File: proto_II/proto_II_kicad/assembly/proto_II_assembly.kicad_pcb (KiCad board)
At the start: 2 copper layers, 100 x 97 mm, 109 parts, among them J101 BOOT_CFG, J102 SNSR_I2C, J103 SNSR_PWR, J104 Vin, J105 RS485_A, J106 RS485_B, J107 ISO_GND, J108 Vin-5V, J109 SWD_DBG, J301 SIG_BYPASS, J302 PWR_BYPASS, SW101 RST, SW102 MODBUS_ADDR, SW103 USR_BTN, U101 STM32F103C8Tx, U201 TPS54331, U202 XC6206P332MR, U301 ADUM5241, U302 EL357N-G, U303 EL357N-G, U304 ST485EBDR, Y101 HSE, Y102 LSE

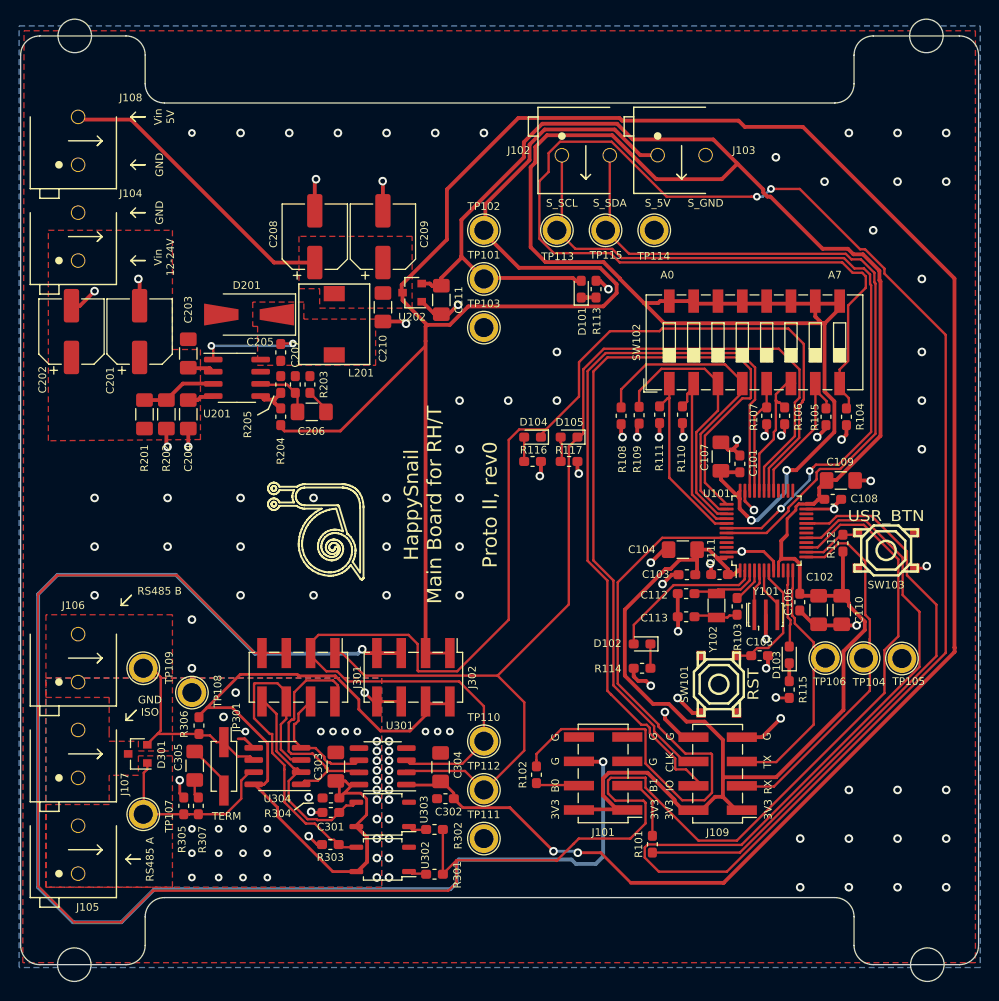
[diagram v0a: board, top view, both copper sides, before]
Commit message: Fix issues with rev.0 of MarkI board
Partially addresses #16
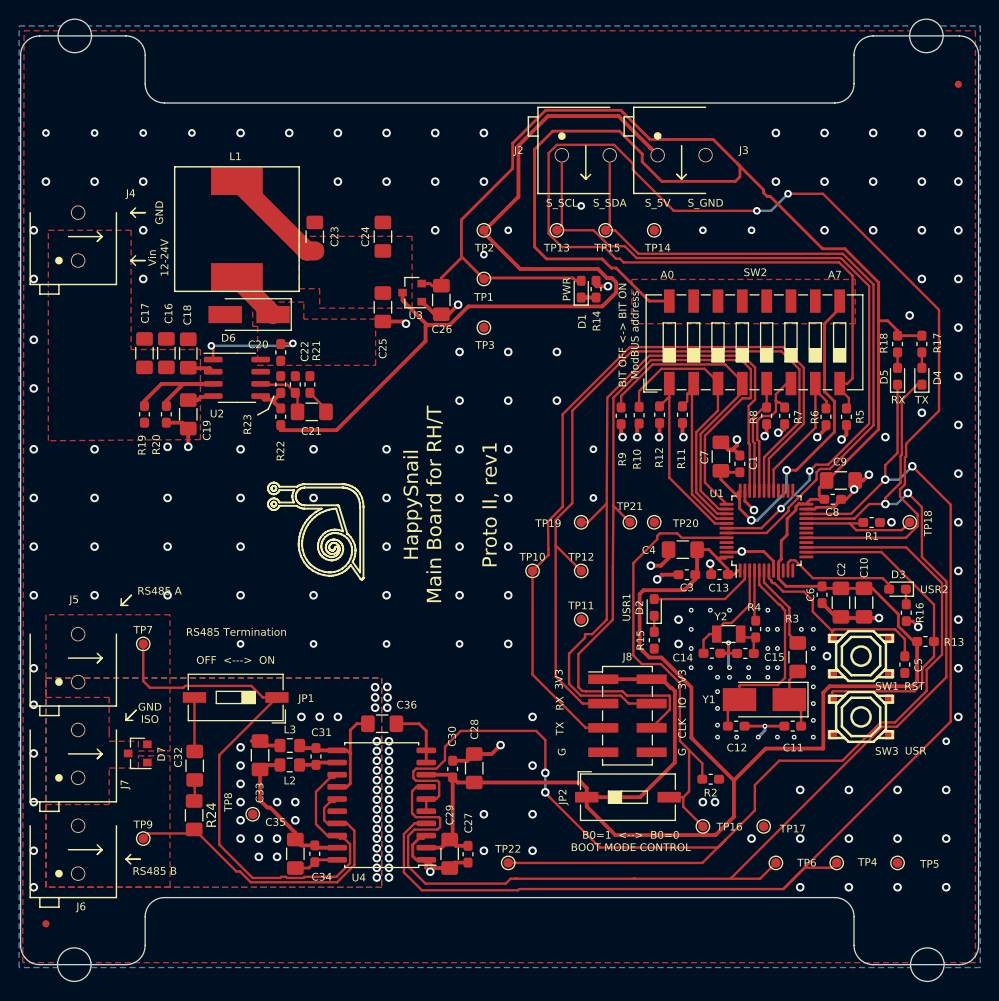
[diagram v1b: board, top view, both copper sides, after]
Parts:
- removed C112: 10p, Capacitor_SMD:C_0603_1608Metric_Pad1.05x0.95mm_HandSolder
- removed C301, C302: 100n, Capacitor_SMD:C_0603_1608Metric_Pad1.05x0.95mm_HandSolder
- removed C303, C304: 1u, Capacitor_SMD:C_1206_3216Metric_Pad1.42x1.75mm_HandSolder
- removed C305: 10n, Capacitor_SMD:C_1206_3216Metric_Pad1.42x1.75mm_HandSolder
- removed D104: DI_LED, Diode_SMD:D_0603_1608Metric_Pad1.05x0.95mm_HandSolder
- removed D105: RO_LED, Diode_SMD:D_0603_1608Metric_Pad1.05x0.95mm_HandSolder
- removed D301: SM712, Package_TO_SOT_SMD:SOT-23
- removed J101: BOOT_CFG, Connector_PinHeader_2.54mm:PinHeader_2x04_P2.54mm_Vertical_SMD
- removed J105: RS485_A, Project:DG300-5.0-02P-12
- removed J106: RS485_B, Project:DG300-5.0-02P-12
- removed J108: Vin-5V, Project:DG300-5.0-02P-12
- removed J301: SIG_BYPASS, Connector_PinHeader_2.54mm:PinHeader_2x04_P2.54mm_Vertical_SMD
- removed J302: PWR_BYPASS, Connector_PinHeader_2.54mm:PinHeader_2x04_P2.54mm_Vertical_SMD
- removed R101, R102, R112, R303, R304: 10K, Resistor_SMD:R_0603_1608Metric_Pad1.05x0.95mm_HandSolder
- removed R103: 0R, Resistor_SMD:R_0603_1608Metric_Pad1.05x0.95mm_HandSolder
- removed R116, R117, R301, R302, R305, R306: 2K2, Resistor_SMD:R_0603_1608Metric_Pad1.05x0.95mm_HandSolder
- removed SW101: RST, Project:Tactile_Switch_5x5mm
- removed SW103: USR_BTN, Project:Tactile_Switch_5x5mm
- removed TP104: U2_RX, TestPoint:TestPoint_Plated_Hole_D2.0mm
- removed TP112: U1_TX, TestPoint:TestPoint_Plated_Hole_D2.0mm
- removed U301: ADUM5241, Package_SO:SOIC-8_3.9x4.9mm_P1.27mm
- removed U302, U303: EL357N-G, Package_SO:SOP-4_3.8x4.1mm_P2.54mm
- removed U304: ST485EBDR, Package_SO:SOIC-8_3.9x4.9mm_P1.27mm
- removed Y101: HSE, Project:Murata_CSTCE8M0V53-R0-3Pin_3.2x1.1mm_HandSoldering
- added C11: 30p, Capacitor_SMD:C_0603_1608Metric_Pad1.05x0.95mm_HandSolder, F.Cu at (118.6, 105.1)
- added C12: 30p, Capacitor_SMD:C_0603_1608Metric_Pad1.05x0.95mm_HandSolder, F.Cu at (112.7, 105.1)
- added C14: 10p, Capacitor_SMD:C_0603_1608Metric_Pad1.05x0.95mm_HandSolder, F.Cu at (110.2, 97.5)
- added C27: 100n, Capacitor_SMD:C_0603_1608Metric_Pad1.05x0.95mm_HandSolder, F.Cu at (84.7, 118.5)
- added C28: 10u, Capacitor_SMD:C_1206_3216Metric_Pad1.42x1.75mm_HandSolder, F.Cu at (85.3, 109.5)
- added C29: 10n, Capacitor_SMD:C_1206_3216Metric_Pad1.42x1.75mm_HandSolder, F.Cu at (82.8, 118.4)
- added C30: 100n, Capacitor_SMD:C_0603_1608Metric_Pad1.05x0.95mm_HandSolder, F.Cu at (83.1, 109.6)
- added C31: 100n, Capacitor_SMD:C_0603_1608Metric_Pad1.05x0.95mm_HandSolder, F.Cu at (68.8, 108.3)
- added C32: 10n, Capacitor_SMD:C_1206_3216Metric_Pad1.42x1.75mm_HandSolder, F.Cu at (56.2, 109.2)
- added C33: 10u, Capacitor_SMD:C_1206_3216Metric_Pad1.42x1.75mm_HandSolder, F.Cu at (63.0, 108.1)
- added C34: 100n, Capacitor_SMD:C_0603_1608Metric_Pad1.05x0.95mm_HandSolder, F.Cu at (68.7, 118.4)
- added C35: 10n, Capacitor_SMD:C_1206_3216Metric_Pad1.42x1.75mm_HandSolder, F.Cu at (66.7, 118.4)
- added C36: 10n, Capacitor_SMD:C_1206_3216Metric_Pad1.42x1.75mm_HandSolder, F.Cu at (75.7, 104.9)
- added D4: BLUE_LED, Diode_SMD:D_0603_1608Metric_Pad1.05x0.95mm_HandSolder, F.Cu at (132.1, 68.6)
- added D5: BLUE_LED, Diode_SMD:D_0603_1608Metric_Pad1.05x0.95mm_HandSolder, F.Cu at (129.5, 68.6)
- added D7: SM712, Package_TO_SOT_SMD:SOT-23, F.Cu at (50.2, 108.0)
- added J5: RS485_A, Project:DG300-5.0-02P-12, F.Cu at (44.0, 98.0)
- added J6: RS485_B, Project:DG300-5.0-02P-12, F.Cu at (44.0, 118.0)
- added JP2: JP, Button_Switch_SMD:SW_DIP_SPSTx01_Slide_9.78x4.72mm_W8.61mm_P2.54mm, F.Cu at (101.4, 112.5)
- added L2: FB, Inductor_SMD:L_0805_2012Metric_Pad1.15x1.40mm_HandSolder, F.Cu at (66.1, 109.2)
- added L3: FB, Inductor_SMD:L_0805_2012Metric_Pad1.15x1.40mm_HandSolder, F.Cu at (66.1, 107.1)
- added R1: 10K, Resistor_SMD:R_0603_1608Metric_Pad1.05x0.95mm_HandSolder, F.Cu at (126.8, 83.8)
- added R13: 10K, Resistor_SMD:R_0603_1608Metric_Pad1.05x0.95mm_HandSolder, F.Cu at (132.5, 96.3)
- added R17: 2K2, Resistor_SMD:R_0603_1608Metric_Pad1.05x0.95mm_HandSolder, F.Cu at (132.1, 65.2)
- added R18: 2K2, Resistor_SMD:R_0603_1608Metric_Pad1.05x0.95mm_HandSolder, F.Cu at (129.5, 65.2)
- added R2: 10K, Resistor_SMD:R_0603_1608Metric_Pad1.05x0.95mm_HandSolder, F.Cu at (110.0, 110.6)
- added R3: 560, Resistor_SMD:R_1206_3216Metric_Pad1.42x1.75mm_HandSolder, F.Cu at (119.1, 97.9)
- added R4: 0R, Resistor_SMD:R_0603_1608Metric_Pad1.05x0.95mm_HandSolder, F.Cu at (114.7, 95.0)
- added REF**: Fiducial_0.75mm_Mask1.5mm, Fiducial:Fiducial_0.75mm_Mask1.5mm, F.Cu at (40.6, 125.7)
- added REF**: Fiducial_0.75mm_Mask1.5mm, Fiducial:Fiducial_0.75mm_Mask1.5mm, F.Cu at (135.9, 38.1)
- added SW1: PB, Project:Tactile_Switch_5x5mm, F.Cu at (125.7, 97.8)
- added SW3: PB, Project:Tactile_Switch_5x5mm, F.Cu at (125.7, 104.1)
- added TP12: U1_TX, TestPoint:TestPoint_Pad_D1.0mm, F.Cu at (96.5, 88.9)
- added TP16: U1_B0, TestPoint:TestPoint_Pad_D1.0mm, F.Cu at (109.2, 115.6)
- added TP17: G_U1, TestPoint:TestPoint_Pad_D1.0mm, F.Cu at (115.6, 115.6)
- added TP18: U1_B1, TestPoint:TestPoint_Pad_D1.0mm, F.Cu at (130.8, 83.8)
- added TP19: U1_B0, TestPoint:TestPoint_Pad_D1.0mm, F.Cu at (96.5, 83.8)
- added TP20: G_U1, TestPoint:TestPoint_Pad_D1.0mm, F.Cu at (104.1, 83.8)
- added TP21: U1_B1, TestPoint:TestPoint_Pad_D1.0mm, F.Cu at (101.6, 83.8)
- added TP22: DE_RE, TestPoint:TestPoint_Pad_D1.0mm, F.Cu at (88.9, 119.4)
- added TP4: U2_RX, TestPoint:TestPoint_Pad_D1.0mm, F.Cu at (123.2, 119.4)
- added U4: ADM2587E, Package_SO:SOIC-20W_7.5x12.8mm_P1.27mm, F.Cu at (75.7, 113.3)
- added Y1: HSE, Crystal:Crystal_SMD_5032-2Pin_5.0x3.2mm_HandSoldering, F.Cu at (115.6, 102.3)
- C16: renamed from C201; footprint Capacitor_SMD:CP_Elec_6.3x5.7 -> Capacitor_SMD:C_1206_3216Metric_Pad1.42x1.75mm_HandSolder
- C17: renamed from C202; footprint Capacitor_SMD:CP_Elec_6.3x5.7 -> Capacitor_SMD:C_1206_3216Metric_Pad1.42x1.75mm_HandSolder
- C23: renamed from C208; value 47u -> 10u; footprint Capacitor_SMD:CP_Elec_6.3x5.7 -> Capacitor_SMD:C_1206_3216Metric_Pad1.42x1.75mm_HandSolder
- C24: renamed from C209; value 47u -> 10u; footprint Capacitor_SMD:CP_Elec_6.3x5.7 -> Capacitor_SMD:C_1206_3216Metric_Pad1.42x1.75mm_HandSolder
- D1: renamed from D101; value PWR_LED -> BLUE_LED
- D2: renamed from D102; value USR1_LED -> BLUE_LED
- D3: renamed from D103; value USR2_LED -> BLUE_LED
- D6: renamed from D201; footprint Diode_SMD:D_SMA-SMB_Universal_Handsoldering -> Diode_SMD:D_SMA_Handsoldering
- JP1: renamed from JP301; footprint Connector_PinHeader_2.54mm:PinHeader_2x01_P2.54mm_Vertical_SMD -> Button_Switch_SMD:SW_DIP_SPSTx01_Slide_9.78x4.72mm_W8.61mm_P2.54mm
- L1: renamed from L201; value 22u -> 47u; footprint Project:CDRH74 -> Project:SWRB1205S
- R19: renamed from R201; footprint Resistor_SMD:R_1206_3216Metric_Pad1.42x1.75mm_HandSolder -> Resistor_SMD:R_0603_1608Metric_Pad1.05x0.95mm_HandSolder
- R20: renamed from R202; footprint Resistor_SMD:R_1206_3216Metric_Pad1.42x1.75mm_HandSolder -> Resistor_SMD:R_0603_1608Metric_Pad1.05x0.95mm_HandSolder
- R24: renamed from R307; footprint Resistor_SMD:R_0603_1608Metric_Pad1.05x0.95mm_HandSolder -> Resistor_SMD:R_1206_3216Metric_Pad1.42x1.75mm_HandSolder
- TP1: renamed from TP101; footprint TestPoint:TestPoint_Plated_Hole_D2.0mm -> TestPoint:TestPoint_Pad_D1.0mm
- TP10: renamed from TP110; footprint TestPoint:TestPoint_Plated_Hole_D2.0mm -> TestPoint:TestPoint_Pad_D1.0mm
- TP11: renamed from TP111; footprint TestPoint:TestPoint_Plated_Hole_D2.0mm -> TestPoint:TestPoint_Pad_D1.0mm
- TP13: renamed from TP113; footprint TestPoint:TestPoint_Plated_Hole_D2.0mm -> TestPoint:TestPoint_Pad_D1.0mm
- TP14: renamed from TP114; footprint TestPoint:TestPoint_Plated_Hole_D2.0mm -> TestPoint:TestPoint_Pad_D1.0mm
- TP15: renamed from TP115; footprint TestPoint:TestPoint_Plated_Hole_D2.0mm -> TestPoint:TestPoint_Pad_D1.0mm
- TP2: renamed from TP102; footprint TestPoint:TestPoint_Plated_Hole_D2.0mm -> TestPoint:TestPoint_Pad_D1.0mm
- TP3: renamed from TP103; footprint TestPoint:TestPoint_Plated_Hole_D2.0mm -> TestPoint:TestPoint_Pad_D1.0mm
- TP5: renamed from TP105; footprint TestPoint:TestPoint_Plated_Hole_D2.0mm -> TestPoint:TestPoint_Pad_D1.0mm
- TP6: renamed from TP106; footprint TestPoint:TestPoint_Plated_Hole_D2.0mm -> TestPoint:TestPoint_Pad_D1.0mm
- TP7: renamed from TP107; footprint TestPoint:TestPoint_Plated_Hole_D2.0mm -> TestPoint:TestPoint_Pad_D1.0mm
- TP8: renamed from TP108; footprint TestPoint:TestPoint_Plated_Hole_D2.0mm -> TestPoint:TestPoint_Pad_D1.0mm
- TP9: renamed from TP109; footprint TestPoint:TestPoint_Plated_Hole_D2.0mm -> TestPoint:TestPoint_Pad_D1.0mm
- moved TP11 25.0 mm to (96.5, 94.0)
- moved TP6 22.0 mm to (116.8, 119.4)
- moved TP5 21.3 mm to (129.5, 119.4)
- moved TP10 18.5 mm to (91.4, 88.9)
- moved TP7 17.8 mm to (50.8, 96.5)
- moved TP9 17.8 mm to (50.8, 116.8)
- moved C5 15.2 mm to (130.3, 98.7), turned to 270 degrees
- moved R16 14.6 mm to (130.5, 93.3)
- moved L1 14.2 mm to (60.6, 53.2), turned to 90 degrees
- moved TP8 14.2 mm to (62.2, 114.3)
- moved D3 13.2 mm to (129.5, 90.8), turned to 180 degrees
- moved J8 11.2 mm to (101.3, 104.0), turned to 0 degrees
- moved C17 7.95 mm to (50.9, 66.2)
- moved JP1 7.29 mm to (60.5, 102.1), turned to 180 degrees
- moved C15 7.27 mm to (113.7, 97.5)
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- renumbered C101 to C1, C110 to C10, C111 to C13, C113 to C15, C203 to C18, C204 to C19, C102 to C2, C205 to C20, C206 to C21, C207 to C22, C210 to C25, C211 to C26, C103 to C3, C104 to C4, C105 to C5, C106 to C6, C107 to C7, C108 to C8, C109 to C9, J102 to J2, J103 to J3, J104 to J4, J107 to J7, J109 to J8, R109 to R10, R110 to R11, R111 to R12, R113 to R14, R114 to R15, R115 to R16, R203 to R21, R204 to R22, R205 to R23, R104 to R5, R105 to R6, R106 to R7, R107 to R8, R108 to R9, SW102 to SW2, U101 to U1, U201 to U2, U202 to U3, Y102 to Y2
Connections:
- J8 pad 3: /UART2_RX -> /UART1_RX
- J8 pad 5: /UART2_TX -> /UART1_TX
- JP1 pad 1: /RS485_B -> /RS485_A
- R24 pad 2: /RS485_A -> /RS485_B
- TP6 pad 1: /UART2_TX -> /UART3_TX
- U1 pad 12: /UART2_TX -> (no net)
- U1 pad 13: /UART2_RX -> (no net)
- U1 pad 21: (no net) -> /UART3_TX
- U1 pad 22: (no net) -> /UART3_RX
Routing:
- net +5V: track 344.2 -> 103.0 mm, vias 2 -> 0
- net GND: track 248.0 -> 97.0 mm, vias 106 -> 213
- net /UART3_TX: track 0.00 -> 133.4 mm, vias 0 -> 2
- net /UART3_RX: track 0.00 -> 130.5 mm, vias 0 -> 2
- net /MODBUS_A7: track 248.6 -> 144.6 mm
- net +5VD: track 80.4 -> 0.00 mm
- net /DE~RE: track 211.2 -> 131.9 mm, vias 0 -> 2
- net /UART1_TX: track 136.1 -> 81.5 mm
- net /BOOT1: track 62.7 -> 12.9 mm
- net /RS485_A: track 19.6 -> 64.9 mm
- net /UART2_RX: track 43.5 -> 0.00 mm
- net /UART1_RX: track 116.2 -> 79.6 mm
- net /rs485/DE_XMTR: track 35.5 -> 0.00 mm
- net /USR_BTN: track 6.06 -> 34.8 mm
- net /UART2_TX: track 27.7 -> 0.00 mm
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- added copper zone on F.Cu, net +3V3
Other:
- net class PWR_THICK added: clearance 0.2, trace_width 0.4, via_dia 0.9, via_drill 0.5
- rule via_min_drill: 0.3 -> 0.25
- board text added: "B0=1 <--> B0=0 BOOT MODE CONTROL"
- board text added: "BIT OFF <-> BIT ON ModBUS address"
- board text added: "OFF <---> ON"
- board text added: "Proto II, rev1"
- board text added: "RS485 Termination"
- board text removed: "B0"
- board text removed: "B1"
- board text removed: "Proto II, rev0"
- board text removed: "TERM"
- board text removed: "Vin 5V"
